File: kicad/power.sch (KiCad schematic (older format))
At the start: 19 parts, among them CON23 PS-ON, CON24 CON6, CON25 FAN, Q7 FDC6401N, Q8 FDC6401N

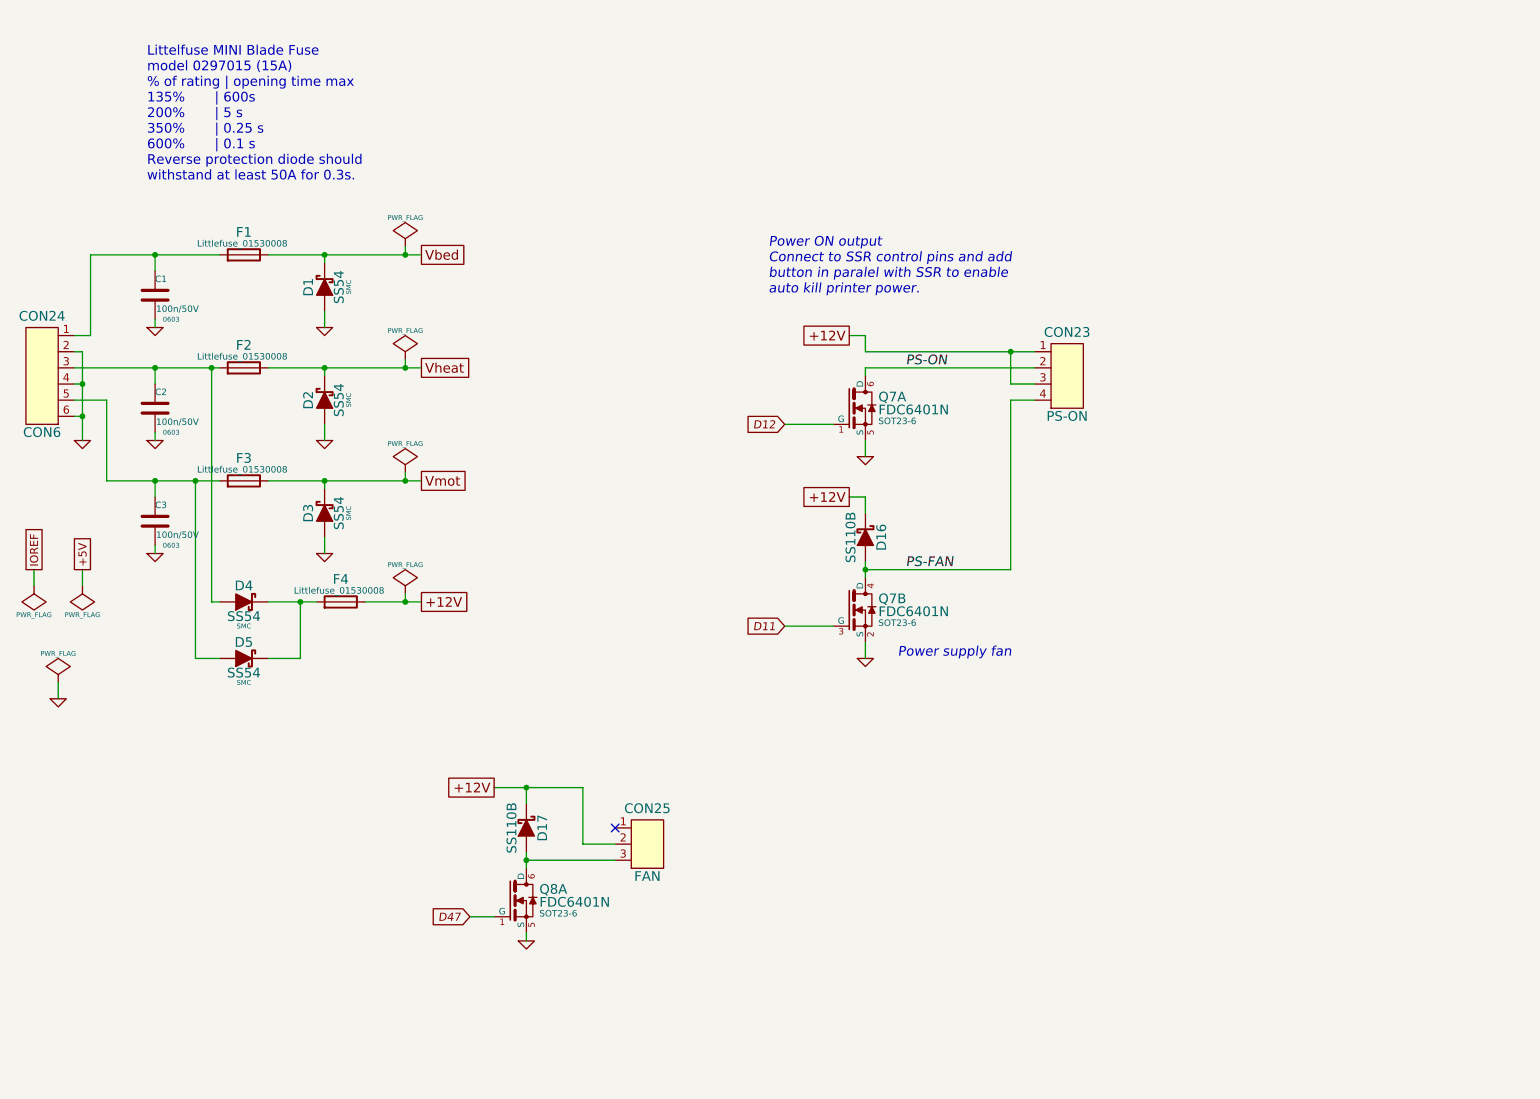
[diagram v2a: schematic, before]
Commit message: Add heated chamber support
close #22
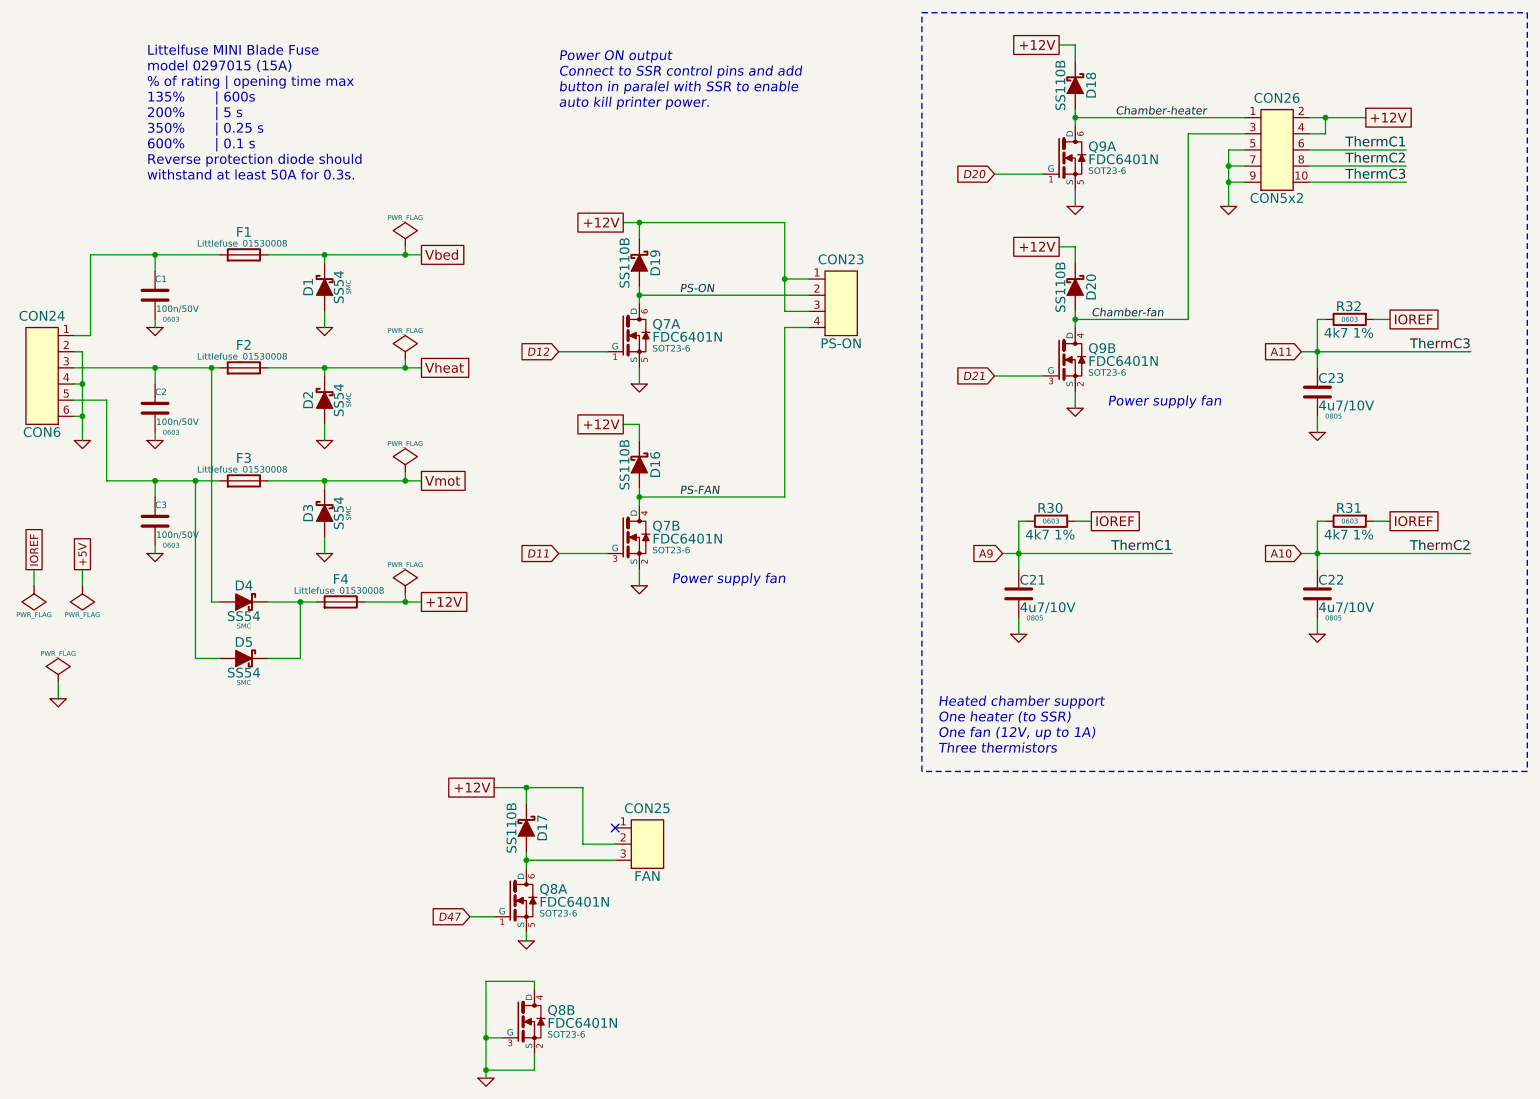
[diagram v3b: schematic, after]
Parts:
- added C21, C22, C23: 4u7/10V, 0805, symbol C
- added CON26: CON5x2, symbol CON5x2
- added D18, D19, D20: SS110B, symbol SS110B
- added unit 2 of Q8
- added Q9: FDC6401N, SOT23-6, symbol FDC6401N
- added R30, R31, R32: 4k7 1%, 0603, symbol R
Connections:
- net +12V: now also CON26.2, CON26.4, D18.1, D19.1, D20.1
- net GND: now also C21.2, C22.2, C23.2, CON26.5, CON26.7, CON26.9, Q8.2 (S), Q8.3 (G), Q8.4 (D), Q9.2 (S), Q9.5 (S)
- net IOREF: now also R30.1, R31.1, R32.1
- net PS-ON: now also D19.2
- new net A10: C22.1, CON26.8, R31.2
- new net A11: C23.1, CON26.10, R32.2
- new net A9: C21.1, CON26.6, R30.2
- new net Chamber-fan: CON26.3, D20.2, Q9.4 (D)
- new net Chamber-heater: CON26.1, D18.2, Q9.6 (D)
- new net D20: Q9.1 (G)
- new net D21: Q9.3 (G)
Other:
- note added: "Heated chamber support\nOne heater (to SSR)\nOne fan (12V, up to 1A)\nThree thermistors"
- moved on the sheet: CON23, D16, Q7A, Q7B

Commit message: Add footprint informations
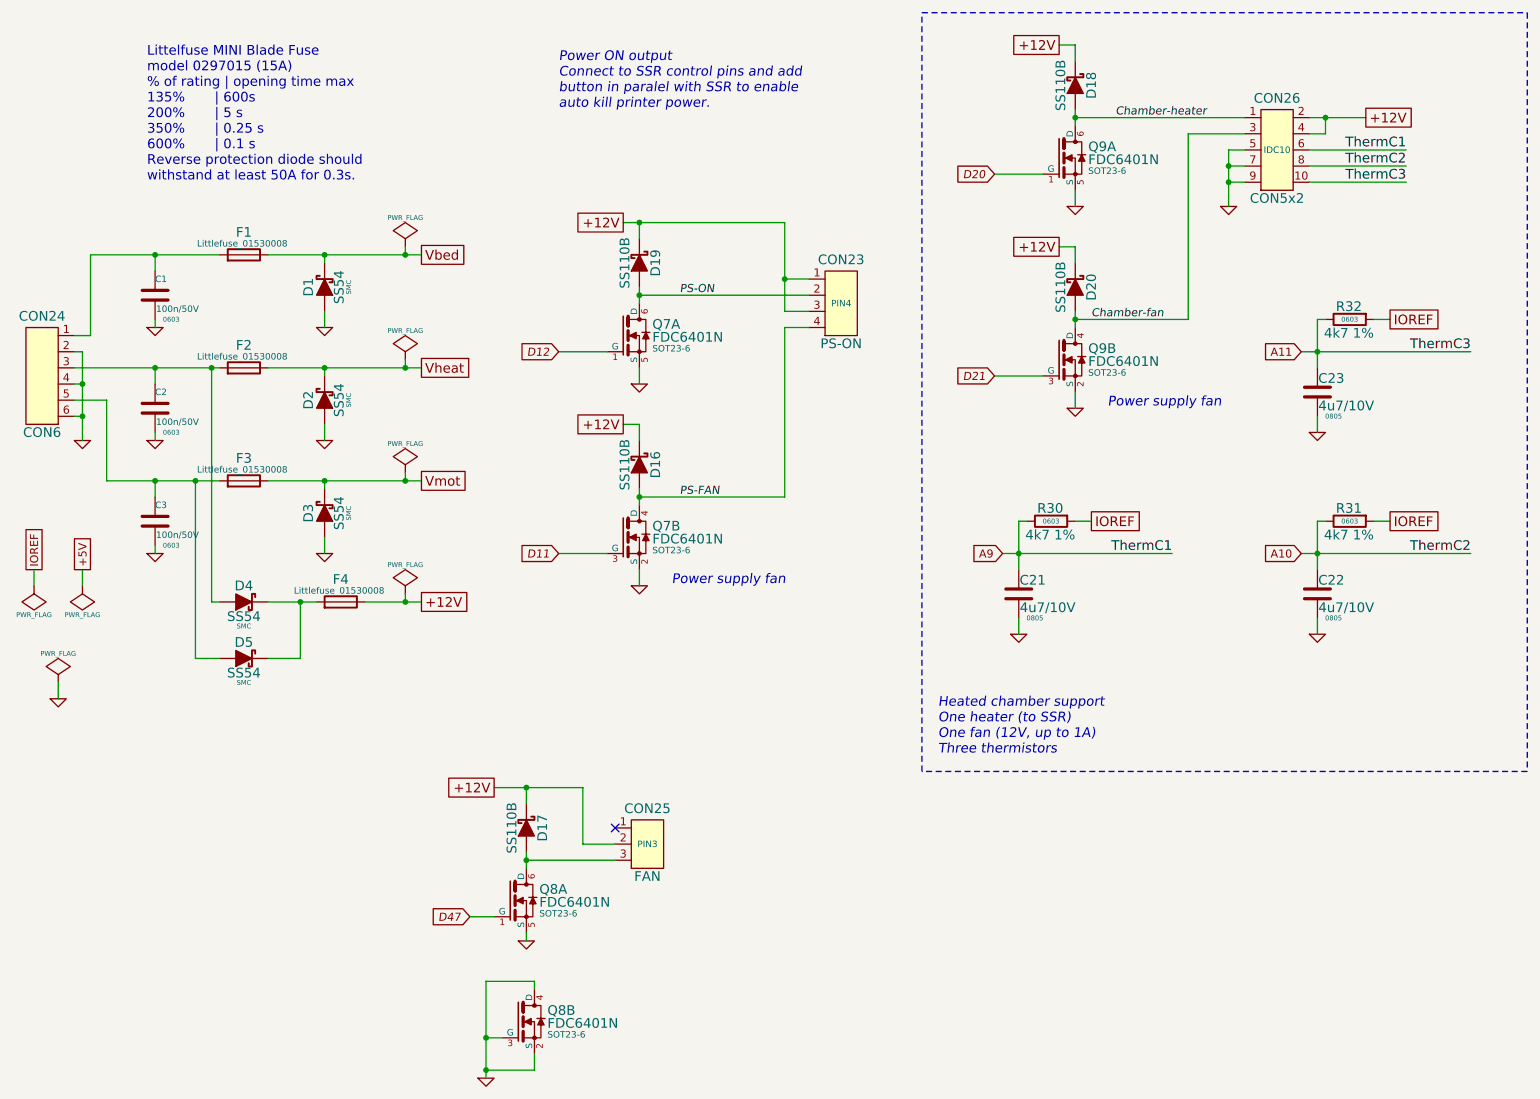
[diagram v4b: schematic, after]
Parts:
- CON23: footprint (none) -> PIN4
- CON25: footprint (none) -> PIN3
- CON26: footprint (none) -> IDC10
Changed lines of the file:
@@
 F 0 "CON23" H 6100 2670 60  0000 C CNN
 F 1 "PS-ON" H 6100 2150 60  0000 C CNN
-F 2 "" H 6100 2400 40  0000 C CNN
+F 2 "PIN4" H 6100 2400 40  0000 C CNN
 F 3 "" H 6100 2400 40  0000 C CNN
 	1    6100 2400
@@
 F 0 "CON25" H 4900 5970 60  0000 C CNN
 F 1 "FAN" H 4900 5550 60  0000 C CNN
-F 2 "" H 4900 5750 40  0000 C CNN
+F 2 "PIN3" H 4900 5750 40  0000 C CNN
 F 3 "" H 4900 5750 40  0000 C CNN
 	1    4900 5750
@@
 F 0 "CON26" H 8800 1770 60  0000 C CNN
 F 1 "CON5x2" H 8800 1150 60  0000 C CNN
-F 2 "" H 8800 1450 40  0000 C CNN
+F 2 "IDC10" H 8800 1450 40  0000 C CNN
 F 3 "" H 8800 1450 40  0000 C CNN
 	1    8800 1450
